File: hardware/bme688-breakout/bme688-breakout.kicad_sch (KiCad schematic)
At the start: 35 parts, among them J1 Conn_01x08, J2 Conn_01x04, J3 Qwiic, J4 Qwiic, Q1 BSS138, Q2 BSS138, Q3 BSS138, Q4 BSS138, U1 BME688, U2 AP2112K-3.3

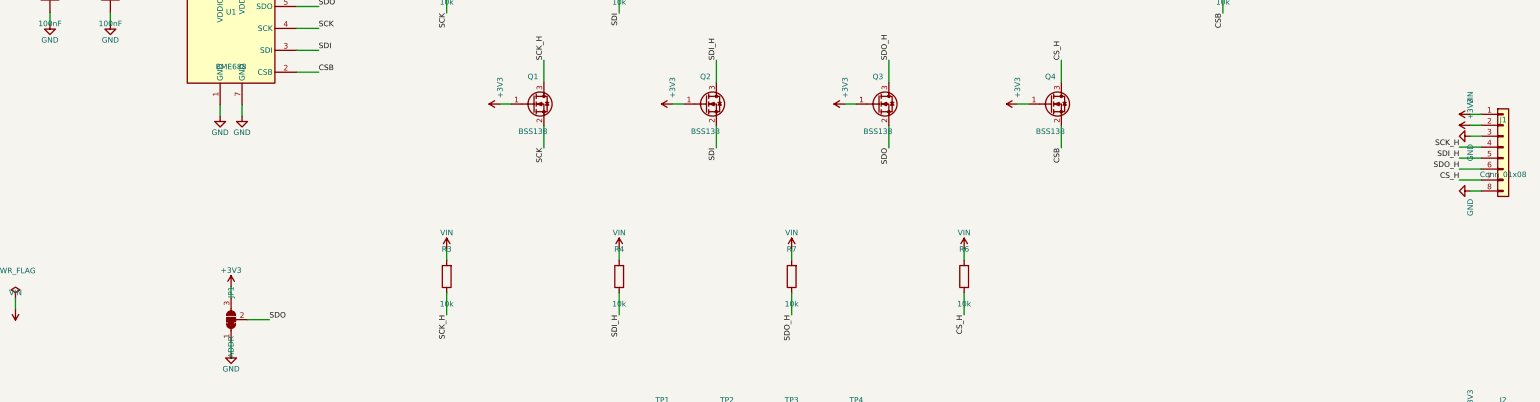
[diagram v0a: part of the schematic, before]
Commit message: Separate VIO from VIN so a 5V-powered board cannot overdrive a 3.3V host
Design review of the level shifters turned up a way to damage the host MCU.
The host-side pull-ups R3/R4/R6/R7 referenced VIN, so the four signal lines
idled at whatever the board was powered from. Run the board off 5V while
talking to a 3.3V part - ESP32, RP2040, STM32, the common case - and SCK,
SDI, SDO and CS all sit at 5V on 3.3V GPIO.

The pull-ups now reference a separate VIO rail, brought out on J1 pin 9
(the host header grows from 8 to 9 pins). JP4 bridges VIO to VIN as
manufactured, so the single-rail cases behave exactly as before and need
nothing done; a mixed-rail host cuts JP4 and feeds VIO from its own I/O
supply.

Also corrects the host logic range, which was claimed as 1.8-5.5V and was
never achievable. A BSS138 shifter needs its gate on the lower of the two
rails and the gate here is on the 3.3V sensor rail, so below 3.3V the FET
body diode (anode at the source, i.e. the sensor side) forward-biases and
pushes about VIO+0.7V back into the host. The real range is 3.3-5.5V;
1.8V logic would need a dual-supply translator, not a different resistor.
The board, silkscreen (front and back) and README all say so now.

VIO is drawn as a rail in the schematic, with its own power symbol in the
project library and a PWR_FLAG, matching how VIN and +3V3 are handled.

Board grows to 36 footprints and 15 nets; JP4 and the wider header are
placed clear of everything, the title moved out from under JP4, and the
whole design re-routed. All checks still pass: net assignment,
connectivity of all 15 nets, the simulated pour (85.8% copper, all 19 GND
items in one region), clearance, courtyards, outline, and the schematic
netlist matching design.py pin for pin.

Co-Authored-By: Claude Opus 5 <noreply@anthropic.com>
Claude-Session: https://claude.ai/code/session_012dyhR133MqMFAMEnBU7Qy6
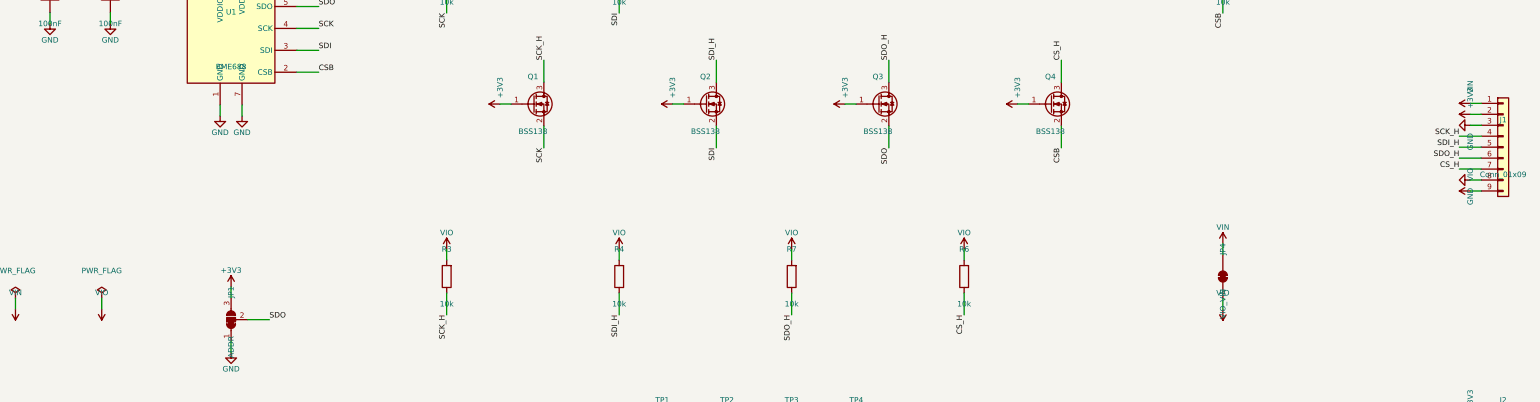
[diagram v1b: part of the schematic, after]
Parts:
- added JP4: VIO_VIN, Jumper:SolderJumper-2_P1.3mm_Bridged_RoundedPad1.0x1.5mm, symbol Jumper:SolderJumper_2_Bridged
- J1: value Conn_01x08 -> Conn_01x09; footprint Connector_PinHeader_2.54mm:PinHeader_1x08_P2.54mm_Vertical -> Connector_PinHeader_2.54mm:PinHeader_1x09_P2.54mm_Vertical; symbol Connector_Generic:Conn_01x08 -> Connector_Generic:Conn_01x09
